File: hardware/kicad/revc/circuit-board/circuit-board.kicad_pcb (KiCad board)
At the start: 2 copper layers, 120 x 175 mm, 242 parts, among them K1 G6K-2F-Y DC5, K2 G6K-2F-Y DC5, K3 G6K-2F-Y DC5, K4 G6K-2F-Y DC5, K5 G6K-2F-Y DC5, P1 TANK-RET (from tank board), P2 WET-OUT (to io-board), P3 FB-RET (to tank board), P4 PWR (from power board), P5 CTL-A: HPF quad 50k lin (PTD9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, P6 CTL-B: LPF quad 50k lin (PTD9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, P7 CTL-C: Ext Mix dual 10k lin, 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, P8 CTL-D: switch lines (from con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, P9 CTL-E: Gain dual 10k lin (con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, Q1201 MMBF5457, Q1221 MMBF5457, Q1341 MMBT3906, U101 L78L09, U102 TL072HIDR, U1201 OPA1679IDR, U1301 OPA1679IDR, U1302 OPA1679IDR, U1303 V2181, U1304 V2181, U1305 OPA1679IDR, U201 OPA1679IDR, U202 OPA1679IDR, U301 OPA1679IDR, U302 OPA1679IDR, U402 TL072HIDR

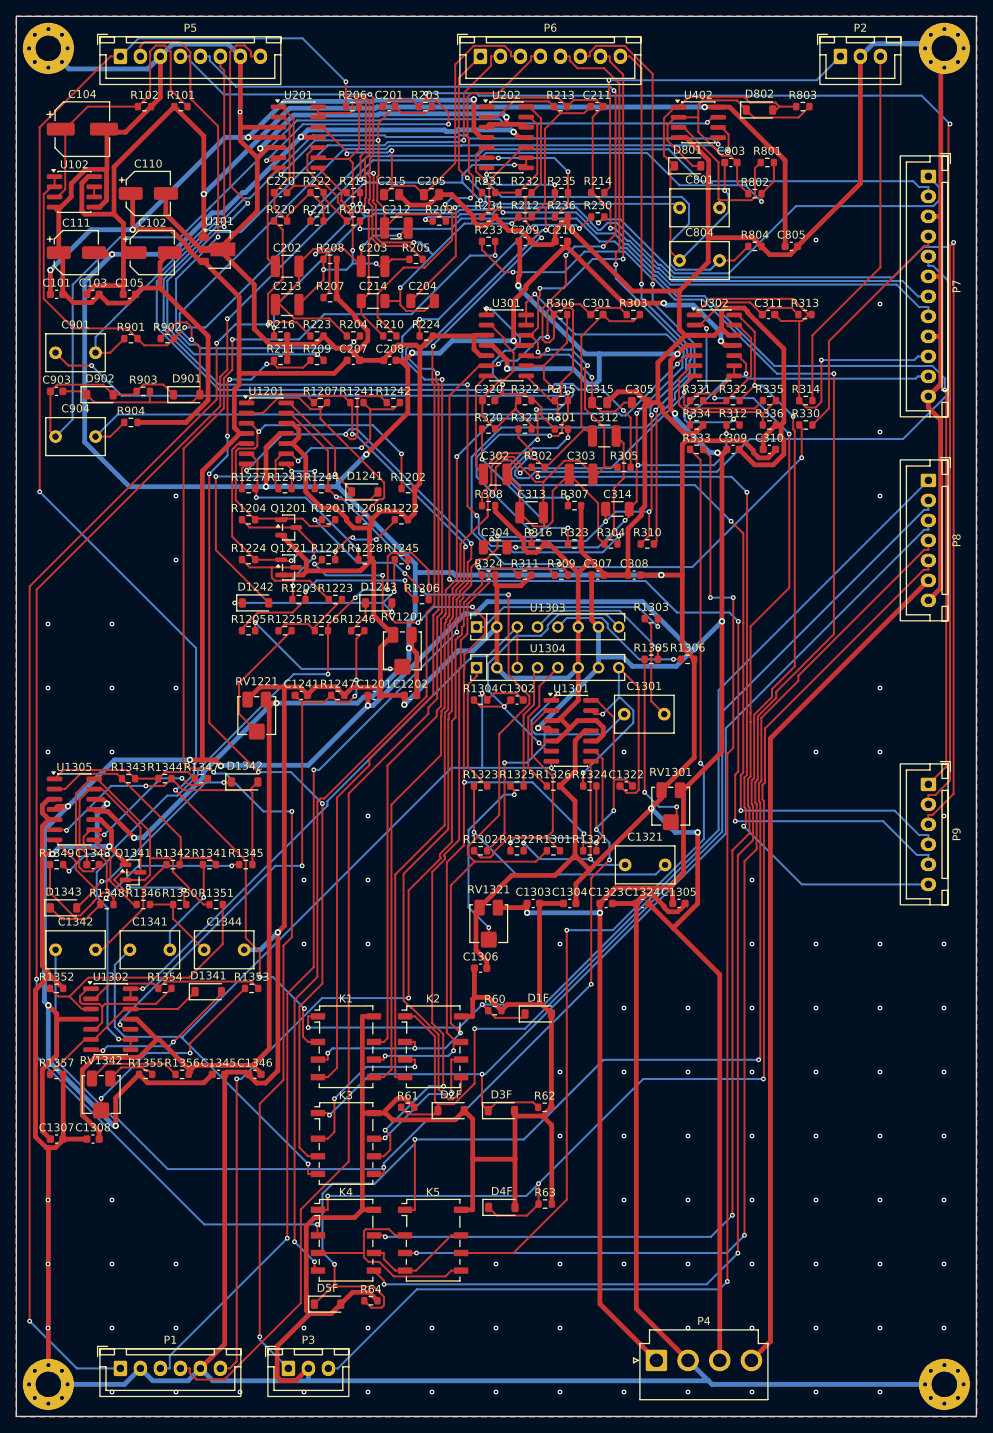
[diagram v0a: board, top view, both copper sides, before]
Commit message: Rev C: Comp/Limit into the feedback return leg, per-mode tank blend knob
Plugin (signal-path diagram v4/v5, 2026-09-30):

- Comp / Off / Limit moves out of the wet path and into the feedback RETURN
  leg, between the Feedback Fb% block and the Fb In summer, so its job is
  holding the loop down rather than shaping what you hear. New
  FeedbackDynamicsBlock carries the circuit plus its oversampling; the wet
  path's DirtDynamicsBlock now always runs Dynamics::off.
- Both thresholds drop 6 dB, kThresholdDbfs -18 -> -24 dBFS, so there is
  something to grab with before the loop is already loud.
- Comp is the MMBF5457 FET model (refs 12xx), not the VTL5C3 vactrol; the
  limiter is a Coolaudio V2181. Stale tooltips corrected.
- Tank blend knob is now per routing: N/A and greyed out in Off, "+ %Long
  Tank" 0-100% linear in Series, "Short / Long Tank Mix" reading
  "x% Short / 100-x% Long" in Parallel. Host automation text matches.
- Per-lane wet predelay ranges (20-30 / 22-35 / 30-42 / 25-40 ms).
- Chain readout: "Fb Out + Comp" / "+ Lim", "In: Tube", and
  "Out: Tube & Tape" so the output tube is visible. The Out knob label only
  looked at Tape before, so it read "Out: Solid State" with the tube in.

Hardware:

- circuit-board re-netted so HPF precedes Gain, matching the schematic
  annotation; ERC 0, Freerouting clean, DRC 0 unconnected / 0 parity.
- U1303/U1304 are Coolaudio V2181; RV1301/RV1321 symmetry trims fitted.
- Fab exports and docs refreshed; rev-c-hardware-definition.md is the live
  spec, the 09-16 PCB release doc stays as the historical record.
- Signal-path draw.io lineage added (v2 through v5).

Repo hygiene:

- .gitignore now covers the cmake-out trees (~1 GB), agent scratch scripts
  and editor .bak files.
- The origin remote no longer carries an embedded personal access token.

Co-Authored-By: Claude Opus 5 <noreply@anthropic.com>
Claude-Session: https://claude.ai/code/session_01CUj6HcY7Ru31X8UWN7atuH
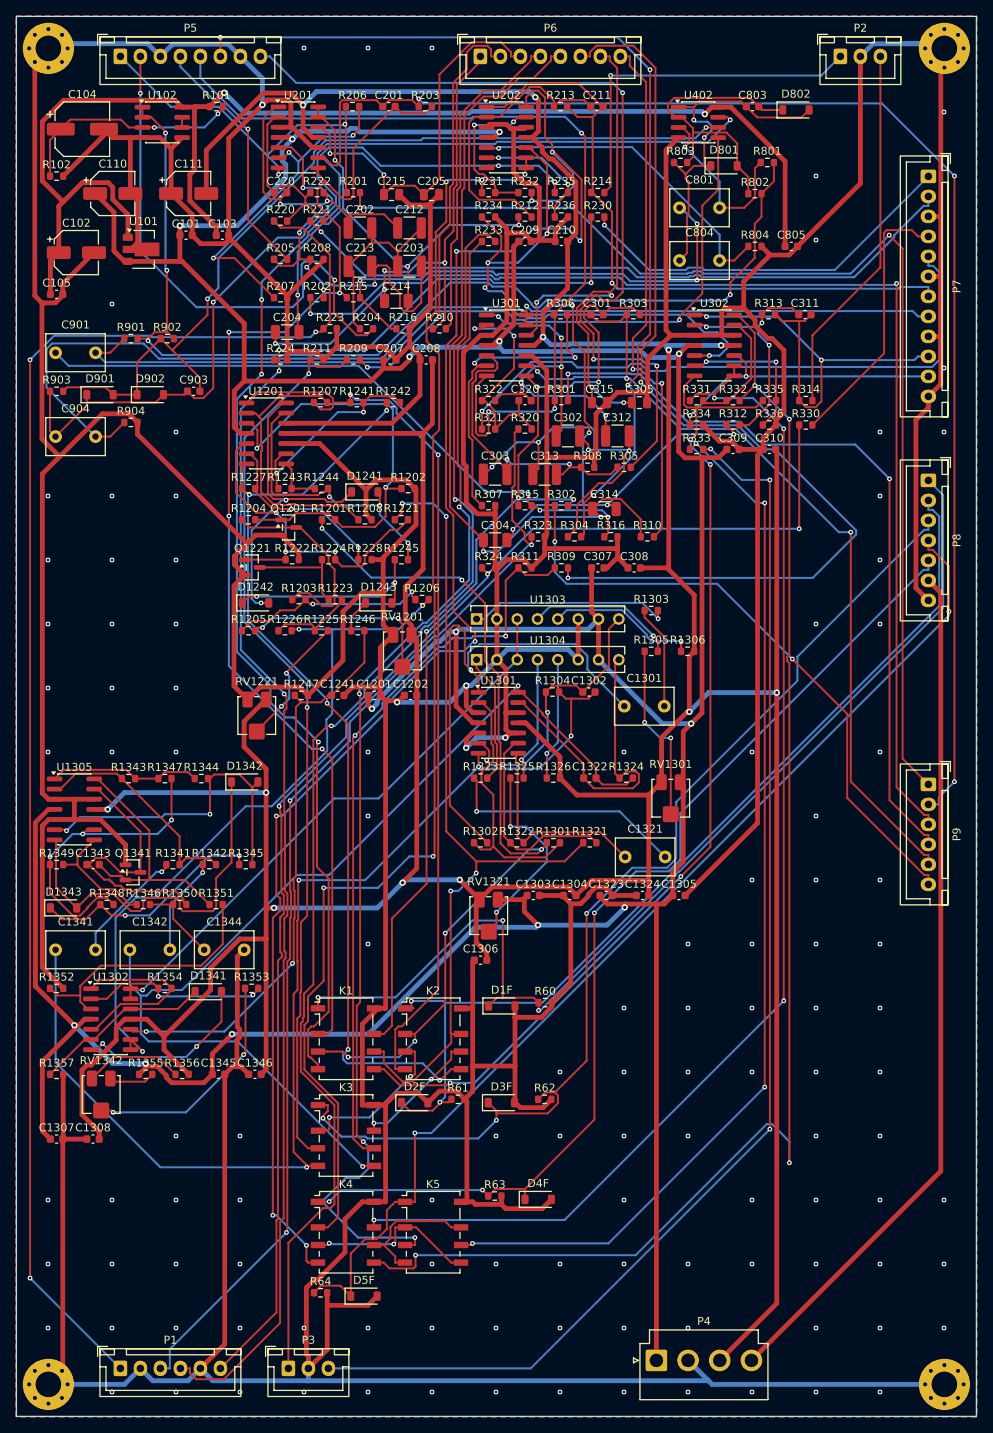
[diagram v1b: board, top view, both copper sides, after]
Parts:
- moved R224 18.4 mm to (33.0, 42.9)
- moved R202 18.0 mm to (37.6, 35.2)
- moved C101 17.8 mm to (21.2, 27.4)
- moved C103 17.8 mm to (25.8, 27.4)
- moved C204 17.4 mm to (33.8, 39.5)
- moved C903 17.1 mm to (22.2, 46.9)
- moved R205 16.9 mm to (33.0, 30.4)
- moved R803 16.8 mm to (83.0, 18.3)
- moved C111 15.9 mm to (21.5, 22.1)
- moved R216 15.3 mm to (48.3, 39.0)
- moved R1222 14.5 mm to (34.5, 67.9)
- moved R102 14.0 mm to (5.03, 20.0)
- moved U102 14.0 mm to (18.2, 13.2)
- moved R315 13.9 mm to (63.6, 61.2)
- moved R308 13.3 mm to (71.4, 56.4)
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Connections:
- C202 pad 1: GAIN_OUT_L -> TANK_MIX_L
- C212 pad 1: GAIN_OUT_L -> TANK_MIX_L
- C302 pad 1: GAIN_OUT_R -> TANK_MIX_R
- C312 pad 1: GAIN_OUT_R -> TANK_MIX_R
- K1 pad 2: HPF_OUT_L -> GAIN_OUT_L
- K1 pad 7: HPF_OUT_R -> GAIN_OUT_R
- R201 pad 1: TANK_MIX_L -> HPF_OUT_L
- R215 pad 1: HPF_OUT_L -> GAIN_OUT_L
- R301 pad 1: TANK_MIX_R -> HPF_OUT_R
- R315 pad 1: HPF_OUT_R -> GAIN_OUT_R
- U201 pad 10: HPF_P_L -> AGND
- U201 pad 5: AGND -> HPF_P_L
- U201 pad 6: GAIN_L_W -> HPF_FB_L
- U201 pad 7: GAIN_OUT_L -> HPF_OUT_L
- U201 pad 8: HPF_OUT_L -> GAIN_OUT_L
- U201 pad 9: HPF_FB_L -> GAIN_L_W
- U301 pad 10: HPF_P_R -> AGND
- U301 pad 5: AGND -> HPF_P_R
- U301 pad 6: GAIN_R_W -> HPF_FB_R
- U301 pad 7: GAIN_OUT_R -> HPF_OUT_R
- U301 pad 8: HPF_OUT_R -> GAIN_OUT_R
- U301 pad 9: HPF_FB_R -> GAIN_R_W
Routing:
- net HPF_OUT_L: track 207.5 -> 49.5 mm, vias 5 -> 2
- net HPF_OUT_R: track 210.7 -> 110.2 mm, vias 5 -> 3
- net GAIN_OUT_L: track 58.6 -> 154.5 mm, vias 2 -> 5
- net GAIN_OUT_R: track 52.3 -> 127.3 mm, vias 0 -> 5
- net AGND: track 1432.8 -> 1502.8 mm, vias 102 -> 118
- net +15VA: track 606.6 -> 538.2 mm, vias 19 -> 14
- net FB_RAW_L: track 209.4 -> 147.5 mm
- net CTL_MEGA: track 172.3 -> 135.8 mm, vias 3 -> 2
- net FB_BUF_L: track 198.7 -> 162.7 mm
- net FB_INV_L: track 162.7 -> 198.8 mm, vias 4 -> 8
- net GAIN_R_W: track 143.5 -> 108.4 mm, vias 5 -> 3
- net LPF_L1_W: track 84.7 -> 53.0 mm
- net TS_DIV_R: track 83.6 -> 114.0 mm
- net VCA_INV_L: track 39.1 -> 65.7 mm, vias 2 -> 1
- net TANK_MIX_R: track 26.3 -> 50.6 mm, vias 2 -> 5
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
